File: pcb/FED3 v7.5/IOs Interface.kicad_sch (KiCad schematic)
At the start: 29 parts, among them IC1 MC74VHC1GT125, Q2 DMP2035U-7

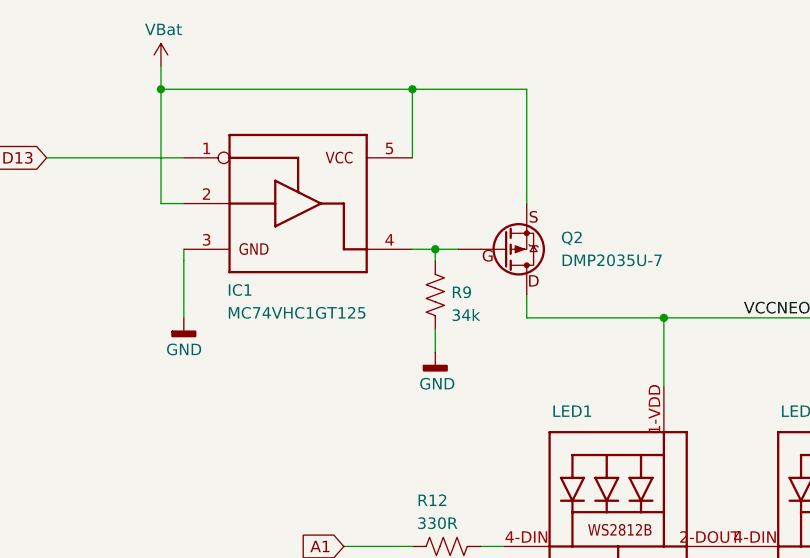
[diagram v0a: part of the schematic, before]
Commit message: FED3 v.7.5 - 1ºs ficheiros de progução
- adicionada header para opção VTherm = Vbat
- optimização para BOM: variedade-vs-quantidade
- optimização de power-planes
- gerados ficheiros produção para 1ª avaliação; há lá erros reconhecidos
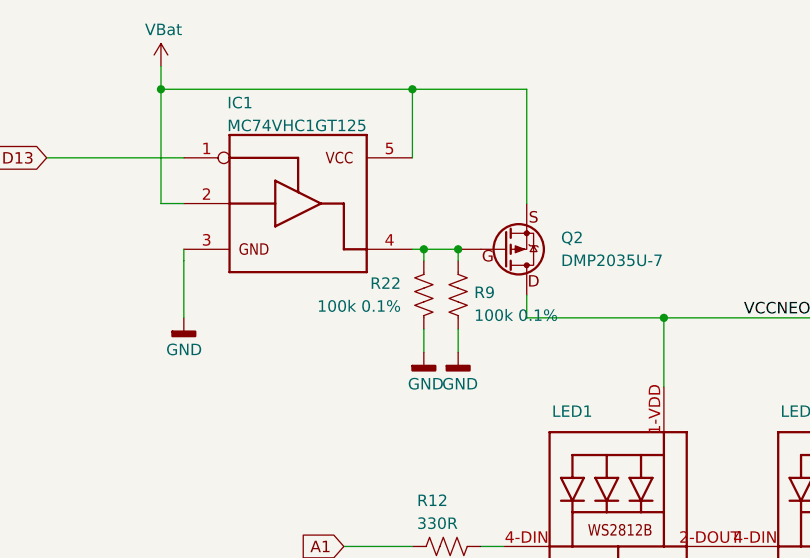
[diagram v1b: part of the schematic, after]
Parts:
- added R22: 100k 0.1%, Resistor_SMD:R_0402_1005Metric, symbol Device:R_US
- R9: value 34k -> 100k 0.1%; MPN RT0402BRD0734KL -> RG1005P-104-B-T5; OEPSPN OEPS020044 -> OEPS020175
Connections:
- net GND: now also R22.1
- net at IC1.4 (P$4), Q2.P$1 (G), R9.2: now also R22.2
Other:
- moved on the sheet: R9
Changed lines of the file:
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@@
 	)
 	(junction
+		(at 68.58 44.45)
+		(diameter 0)
+		(color 0 0 0 0)
+	)
+	(junction
 		(at 142.24 52.07)
 		(diameter 0)
@@
 	)
 	(junction
-		(at 243.84 52.07)
+		(at 64.77 44.45)
 		(diameter 0)
 		(color 0 0 0 0)
 	)
 	(junction
-		(at 63.5 26.67)
+		(at 243.84 52.07)
 		(diameter 0)
 		(color 0 0 0 0)
 	)
 	(junction
-		(at 153.67 27.94)
+		(at 63.5 26.67)
 		(diameter 0)
 		(color 0 0 0 0)
 	)
 	(junction
-		(at 146.05 27.94)
+		(at 153.67 27.94)
 		(diameter 0)
 		(color 0 0 0 0)
 	)
 	(junction
-		(at 66.04 44.45)
+		(at 146.05 27.94)
 		(diameter 0)
 		(color 0 0 0 0)
@@
 	(wire
 		(pts
+			(xy 64.77 53.34) (xy 64.77 55.88)
+		)
+		(stroke
+			(width 0)
+			(type solid)
+		)
+	)
+	(wire
+		(pts
 			(xy 86.36 127) (xy 86.36 129.54)
 		)
@@
 	(wire
 		(pts
-			(xy 66.04 44.45) (xy 66.04 45.72)
+			(xy 68.58 44.45) (xy 68.58 45.72)
 		)
 		(stroke
@@
 	(wire
 		(pts
-			(xy 66.04 44.45) (xy 68.58 44.45)
-		)
-		(stroke
-			(width 0.1524)
-			(type solid)
-		)
-	)
-	(wire
-		(pts
 			(xy 38.1 45.72) (xy 38.1 52.07)
 		)
@@
 	(wire
 		(pts
-			(xy 66.04 53.34) (xy 66.04 55.88)
+			(xy 68.58 53.34) (xy 68.58 55.88)
 		)
 		(stroke
@@
 	(wire
 		(pts
+			(xy 64.77 44.45) (xy 68.58 44.45)
+		)
+		(stroke
+			(width 0.1524)
+			(type solid)
+		)
+	)
+	(wire
+		(pts
 			(xy 63.5 77.47) (xy 55.88 77.47)
 		)
@@
 	(wire
 		(pts
-			(xy 66.04 44.45) (xy 63.5 44.45)
+			(xy 63.5 44.45) (xy 64.77 44.45)
 		)
 		(stroke
@@
 	(wire
 		(pts
+			(xy 64.77 44.45) (xy 64.77 45.72)
+		)
+		(stroke
+			(width 0)
+			(type default)
+		)
+	)
+	(wire
+		(pts
 			(xy 137.16 85.09) (xy 137.16 87.63)
 		)
@@
 	)
 	(symbol
+		(lib_id "power:GNDD")
+		(at 64.77 55.88 0)
+		(unit 1)
+		(exclude_from_sim no)
+		(in_bom yes)
+		(on_board yes)
+		(dnp no)
+		(property "Reference" "#PWR069"
+			(at 64.77 55.88 0)
+			(effects
+				(font
+					(size 1.27 1.27)
+				)
+				(justify bottom)
+				(hide yes)
+			)
+		)
+		(property "Value" "GND"
+			(at 62.992 59.436 0)
+			(effects
+				(font
+					(size 1.27 1.27)
+				)
+				(justify left)
+			)
+		)
+		(property "Footprint" ""
+			(at 64.77 55.88 0)
+			(effects
+				(font
+					(size 1.27 1.27)
+				)
+				(hide yes)
+			)
+		)
+		(property "Datasheet" ""
+			(at 64.77 55.88 0)
+			(effects
+				(font
+					(size 1.27 1.27)
+				)
+				(hide yes)
+			)
+		)
+		(property "Description" "Power symbol creates a global label with name \"GNDD\" , digital ground"
+			(at 64.77 55.88 0)
+			(effects
+				(font
+					(size 1.27 1.27)
+				)
+				(hide yes)
+			)
+		)
+		(pin "1"
+		)
+		(instances
+			(project "FED3"
+				(path "/2ba63f12-2fcd-4471-9636-2762cde37de8/91f92fff-cc86-4ce2-a671-c31760f8020c"
+					(reference "#PWR069")
+					(unit 1)
+				)
+			)
+		)
+	)
+	(symbol
 		(lib_id "power:+3V3")
 		(at 52.07 149.86 0)
@@
 	(symbol
 		(lib_id "power:GNDD")
-		(at 66.04 55.88 0)
+		(at 68.58 55.88 0)
 		(unit 1)
 		(exclude_from_sim no)
@@
 		(dnp no)
 		(property "Reference" "#PWR033"
-			(at 66.04 55.88 0)
+			(at 68.58 55.88 0)
 			(effects
 				(font
@@
 		)
 		(property "Value" "GND"
-			(at 64.262 59.436 0)
+			(at 66.802 59.436 0)
 			(effects
 				(font
@@
 		)
 		(property "Footprint" ""
-			(at 66.04 55.88 0)
+			(at 68.58 55.88 0)
 			(effects
 				(font
@@
 		)
 		(property "Datasheet" ""
-			(at 66.04 55.88 0)
+			(at 68.58 55.88 0)
 			(effects
 				(font
@@
 		)
 		(property "Description" "Power symbol creates a global label with name \"GNDD\" , digital ground"
-			(at 66.04 55.88 0)
+			(at 68.58 55.88 0)
 			(effects
 				(font
@@
 	(symbol
 		(lib_id "Device:R_US")
-		(at 66.04 49.53 180)
+		(at 68.58 49.53 180)
 		(unit 1)
 		(exclude_from_sim no)
@@
 		(dnp no)
 		(property "Reference" "R9"
-			(at 67.818 49.276 0)
+			(at 70.358 49.276 0)
 			(effects
 				(font
@@
 			)
 		)
-		(property "Value" "34k"
-			(at 67.818 51.816 0)
+		(property "Value" "100k 0.1%"
+			(at 70.358 51.816 0)
 			(effects
 				(font
@@
 		)
 		(property "Footprint" "Resistor_SMD:R_0402_1005Metric"
-			(at 66.04 49.53 0)
+			(at 68.58 49.53 0)
 			(effects
 				(font
@@
 		)
 		(property "Datasheet" ""
-			(at 66.04 49.53 0)
+			(at 68.58 49.53 0)
 			(effects
 				(font
@@
 		)
 		(property "Description" "SMD 0402 34kΩ ±0.1% 0.063W"
-			(at 66.04 49.53 0)
+			(at 68.58 49.53 0)
 			(effects
 				(font
@@
 			)
 		)
-		(property "OEPSPN" "OEPS020044"
-			(at 66.04 49.53 0)
+		(property "OEPSPN" "OEPS020175"
+			(at 68.58 49.53 0)
 			(effects
 				(font
@@
 			)
 		)
-		(property "MPN" "RT0402BRD0734KL"
-			(at 66.04 49.53 0)
+		(property "MPN" "RG1005P-104-B-T5"
+			(at 68.58 49.53 0)
 			(effects
 				(font
@@
 	)
 	(symbol
+		(lib_id "Device:R_US")
+		(at 64.77 49.53 0)
+		(mirror x)
+		(unit 1)
+		(exclude_from_sim no)
+		(in_bom yes)
+		(on_board yes)
+		(dnp no)
+		(property "Reference" "R22"
+			(at 62.23 48.2599 0)
+			(effects
+				(font
+					(size 1.27 1.27)
+				)
+				(justify right)
+			)
+		)
+		(property "Value" "100k 0.1%"
+			(at 62.23 50.7999 0)
+			(effects
+				(font
+					(size 1.27 1.27)
+				)
+				(justify right)
+			)
+		)
+		(property "Footprint" "Resistor_SMD:R_0402_1005Metric"
+			(at 64.77 49.53 0)
+			(effects
+				(font
+					(size 1.27 1.27)
+				)
+				(hide yes)
+			)
+		)
+		(property "Datasheet" ""
+			(at 64.77 49.53 0)
+			(effects
+				(font
+					(size 1.27 1.27)
+				)
+				(hide yes)
+			)
+		)
+		(property "Description" "SMD 0402 34kΩ ±0.1% 0.063W"
+			(at 64.77 49.53 0)
+			(effects
+				(font
+					(size 1.27 1.27)
+				)
+				(hide yes)
+			)
+		)
+		(property "OEPSPN" "OEPS020175"
+			(at 64.77 49.53 0)
+			(effects
+				(font
+					(size 1.27 1.27)
+				)
+				(hide yes)
+			)
+		)
+		(property "MPN" "RG1005P-104-B-T5"
+			(at 64.77 49.53 0)
+			(effects
+				(font
+					(size 1.27 1.27)
+				)
+				(hide yes)
+			)
+		)
+		(pin "2"
+		)
+		(pin "1"
+		)
+		(instances
+			(project "FED3"
+				(path "/2ba63f12-2fcd-4471-9636-2762cde37de8/91f92fff-cc86-4ce2-a671-c31760f8020c"
+					(reference "R22")
+					(unit 1)
+				)
+			)
+		)
+	)
+	(symbol
 		(lib_id "FED3 SymbLib:WS2812B5050")
 		(at 264.16 114.3 0)
@@
 		(dnp no)
 		(property "Reference" "IC1"
-			(at 42.926 49.022 0)
+			(at 42.926 28.194 0)
 			(effects
 				(font
@@
 		)
 		(property "Value" "MC74VHC1GT125"
-			(at 42.926 51.562 0)
+			(at 42.926 30.734 0)
 			(effects
 				(font
